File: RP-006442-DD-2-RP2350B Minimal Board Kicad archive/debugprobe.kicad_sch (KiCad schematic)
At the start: 41 parts, among them J4 Conn_01x03, J5 USB_C_Receptacle_USB2.0_16P, SW3 SW_Push, SW4 SW_Push, SW9 SW_SPDT, U5 W25Q128JVS, U6 NCP1117-3.3_SOT223, U7 RP2350_60QFN, Y2 ABM8-272-T3

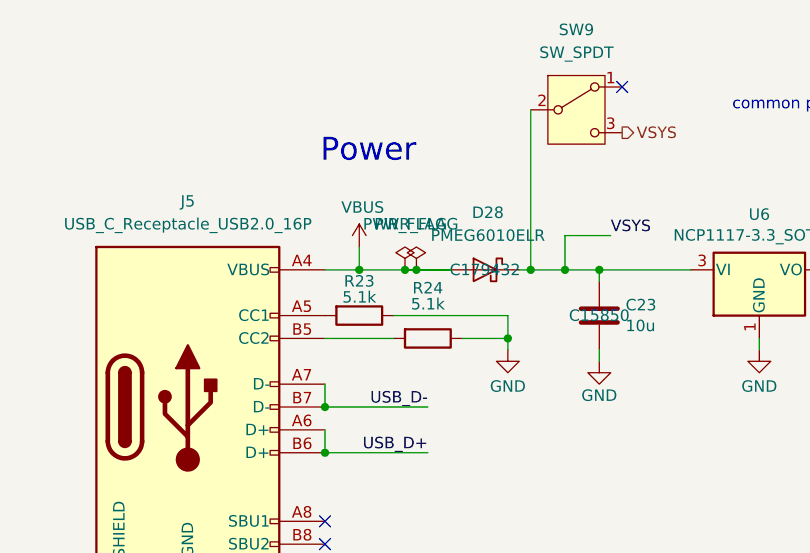
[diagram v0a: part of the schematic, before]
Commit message: Update GS3011CR-G footprint
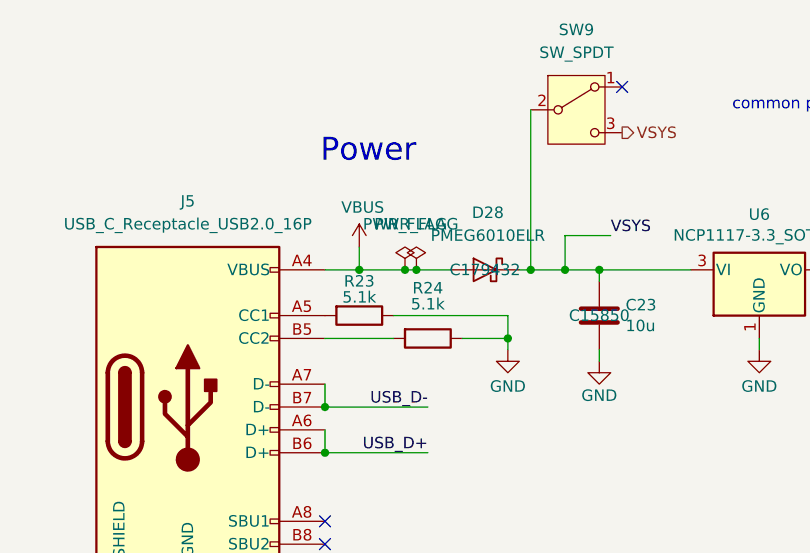
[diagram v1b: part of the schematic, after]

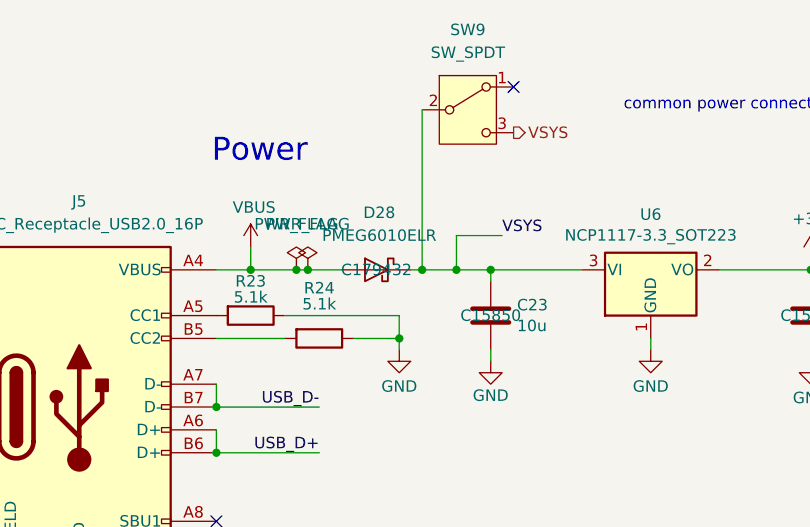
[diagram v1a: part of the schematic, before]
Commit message: Update hex display pcb traces
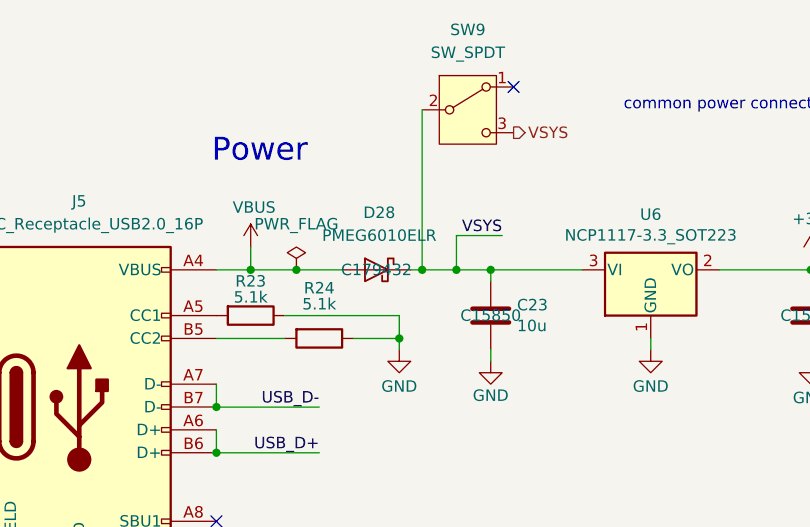
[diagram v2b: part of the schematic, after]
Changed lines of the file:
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@@
 	)
 	(junction
-		(at 76.2 58.42)
-		(diameter 0)
-		(color 0 0 0 0)
-	)
-	(junction
 		(at 209.55 100.33)
 		(diameter 0)
@@
 	)
 	(junction
-		(at 74.93 58.42)
-		(diameter 0)
-		(color 0 0 0 0)
-	)
-	(junction
 		(at 57.15 182.88)
 		(diameter 0)
@@
 	)
 	(junction
+		(at 74.93 58.42)
+		(diameter 0)
+		(color 0 0 0 0)
+	)
+	(junction
 		(at 189.23 90.17)
 		(diameter 0)
@@
 	(wire
 		(pts
-			(xy 76.2 58.42) (xy 80.01 58.42)
+			(xy 69.85 58.42) (xy 74.93 58.42)
 		)
 		(stroke
@@
 	(wire
 		(pts
+			(xy 74.93 58.42) (xy 80.01 58.42)
+		)
+		(stroke
+			(width 0)
+			(type default)
+		)
+	)
+	(wire
+		(pts
 			(xy 292.1 91.44) (xy 280.67 91.44)
 		)
@@
 	(wire
 		(pts
-			(xy 69.85 58.42) (xy 74.93 58.42)
-		)
-		(stroke
-			(width 0)
-			(type default)
-		)
-	)
-	(wire
-		(pts
 			(xy 92.71 58.42) (xy 96.52 58.42)
 		)
@@
 	(wire
 		(pts
-			(xy 74.93 58.42) (xy 76.2 58.42)
-		)
-		(stroke
-			(width 0)
-			(type default)
-		)
-	)
-	(wire
-		(pts
 			(xy 77.47 78.74) (xy 66.04 78.74)
 		)
@@
 	)
 	(label "VSYS"
-		(at 97.79 54.61 0)
+		(at 97.79 54.61 180)
 		(effects
 			(font
 				(size 1.27 1.27)
 			)
-			(justify left bottom)
+			(justify right bottom)
 		)
 	)
@@
 	(symbol
 		(lib_id "power:PWR_FLAG")
-		(at 76.2 58.42 0)
+		(at 74.93 58.42 0)
 		(unit 1)
 		(exclude_from_sim no)
@@
 		(fields_autoplaced yes)
 		(property "Reference" "#FLG02"
-			(at 76.2 56.515 0)
+			(at 74.93 56.515 0)
 			(effects
 				(font
@@
 		)
 		(property "Value" "PWR_FLAG"
-			(at 76.2 53.34 0)
+			(at 74.93 53.34 0)
 			(effects
 				(font
@@
 		)
 		(property "Footprint" ""
-			(at 76.2 58.42 0)
+			(at 74.93 58.42 0)
 			(effects
 				(font
@@
 		)
 		(property "Datasheet" "~"
-			(at 76.2 58.42 0)
+			(at 74.93 58.42 0)
 			(effects
 				(font
@@
 		)
 		(property "Description" "Special symbol for telling ERC where power comes from"
-			(at 76.2 58.42 0)
+			(at 74.93 58.42 0)
 			(effects
 				(font
@@
 		)
 		(instances
-			(project ""
+			(project "RP2350_80QFN_minimal"
 				(path "/94683f5c-9cd9-448e-be96-9792537b5cb8/500e1af8-c8c5-44c6-9fbe-f4d5e5ab4ca8"
 					(reference "#FLG02")
@@
 					(unit 1)
 				)
-			)
-		)
-	)
-	(symbol
-		(lib_id "power:PWR_FLAG")
-		(at 74.93 58.42 0)
-		(unit 1)
-		(exclude_from_sim no)
-		(in_bom yes)
-		(on_board yes)
-		(dnp no)
-		(fields_autoplaced yes)
-		(property "Reference" "#FLG02"
-			(at 74.93 56.515 0)
-			(effects
-				(font
-					(size 1.27 1.27)
-				)
-				(hide yes)
-			)
-		)
-		(property "Value" "PWR_FLAG"
-			(at 74.93 53.34 0)
-			(effects
-				(font
-					(size 1.27 1.27)
-				)
-			)
-		)
-		(property "Footprint" ""
-			(at 74.93 58.42 0)
-			(effects
-				(font
-					(size 1.27 1.27)
-				)
-				(hide yes)
-			)
-		)
-		(property "Datasheet" "~"
-			(at 74.93 58.42 0)
-			(effects
-				(font
-					(size 1.27 1.27)
-				)
-				(hide yes)
-			)
-		)
-		(property "Description" "Special symbol for telling ERC where power comes from"
-			(at 74.93 58.42 0)
-			(effects
-				(font
-					(size 1.27 1.27)
-				)
-				(hide yes)
-			)
-		)
-		(pin "1"
-		)
-		(instances
-			(project ""
-				(path "/94683f5c-9cd9-448e-be96-9792537b5cb8/500e1af8-c8c5-44c6-9fbe-f4d5e5ab4ca8"
-					(reference "#FLG02")
-					(unit 1)
-				)

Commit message: Update
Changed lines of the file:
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@@
 	(text "Power"
 		(exclude_from_sim no)
-		(at 65.532 46.736 0)
+		(at 65.024 42.926 0)
 		(effects
 			(font
@@
 	)
 	(junction
+		(at 162.56 121.92)
+		(diameter 0)
+		(color 0 0 0 0)
+	)
+	(junction
 		(at 212.09 100.33)
 		(diameter 0)
@@
 	(wire
 		(pts
+			(xy 162.56 121.92) (xy 168.91 121.92)
+		)
+		(stroke
+			(width 0)
+			(type default)
+		)
+	)
+	(wire
+		(pts
 			(xy 40.64 182.88) (xy 43.18 182.88)
 		)
@@
 	(wire
 		(pts
-			(xy 153.67 121.92) (xy 168.91 121.92)
+			(xy 153.67 121.92) (xy 162.56 121.92)
 		)
 		(stroke
@@
 					(unit 1)
 				)
+			)
+		)
+	)
+	(symbol
+		(lib_id "power:PWR_FLAG")
+		(at 162.56 121.92 0)
+		(unit 1)
+		(exclude_from_sim no)
+		(in_bom yes)
+		(on_board yes)
+		(dnp no)
+		(fields_autoplaced yes)
+		(property "Reference" "#FLG05"
+			(at 162.56 120.015 0)
+			(effects
+				(font
+					(size 1.27 1.27)
+				)
+				(hide yes)
+			)
+		)
+		(property "Value" "PWR_FLAG"
+			(at 162.56 116.84 0)
+			(effects
+				(font
+					(size 1.27 1.27)
+				)
+			)
+		)
+		(property "Footprint" ""
+			(at 162.56 121.92 0)
+			(effects
+				(font
+					(size 1.27 1.27)
+				)
+				(hide yes)
+			)
+		)
+		(property "Datasheet" "~"
+			(at 162.56 121.92 0)
+			(effects
+				(font
+					(size 1.27 1.27)
+				)
+				(hide yes)
+			)
+		)
+		(property "Description" "Special symbol for telling ERC where power comes from"
+			(at 162.56 121.92 0)
+			(effects
+				(font
+					(size 1.27 1.27)
+				)
+				(hide yes)
+			)
+		)
+		(pin "1"
+		)
+		(instances
+			(project ""
+				(path "/94683f5c-9cd9-448e-be96-9792537b5cb8/500e1af8-c8c5-44c6-9fbe-f4d5e5ab4ca8"
+					(reference "#FLG05")
+					(unit 1)
+				)

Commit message: Update usb power switch
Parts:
- SW9: footprint Button_Switch_SMD:SW_SPDT_HRO_K3-1235S-K1 -> Button_Switch_SMD:SW_SPDT_G-Switch_MK-12C03-G015; LCSC C520835 -> C2890358
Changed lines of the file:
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@@
 			)
 		)
-		(property "Footprint" "Button_Switch_SMD:SW_SPDT_HRO_K3-1235S-K1"
+		(property "Footprint" "Button_Switch_SMD:SW_SPDT_G-Switch_MK-12C03-G015"
 			(at 93.98 40.64 0)
 			(effects
@@
 			)
 		)
-		(property "LCSC" "C520835"
+		(property "LCSC" "C2890358"
 			(at 93.98 40.64 0)
 			(effects

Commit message: Production files
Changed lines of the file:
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@@
 					(size 1.27 1.27)
 				)
-				(hide yes)
 			)
 		)
@@
 			)
 		)
-		(property "LSCS" ""
-			(at 50.8 73.66 0)
-			(effects
-				(font
-					(size 1.27 1.27)
-				)
-			)
-		)
 		(pin "B5"
 		)
@@
 					(size 1.27 1.27)
 				)
-				(hide yes)
 			)
 		)
@@
 			)
 		)
-		(property "LSCS" ""
-			(at 200.66 85.09 0)
-			(effects
-				(font
-					(size 1.27 1.27)
-				)
-			)
-		)
 		(pin "1"
 		)
@@
 					(size 1.27 1.27)
 				)
-				(hide yes)
 			)
 		)
@@
 					(size 1.27 1.27)
 				)
-				(hide yes)
 			)
 		)
@@
 			)
 		)
-		(property "LSCS" ""
-			(at 177.8 85.09 0)
-			(effects
-				(font
-					(size 1.27 1.27)
-				)
-			)
-		)
 		(pin "1"
 		)
@@
 					(size 1.27 1.27)
 				)
-				(hide yes)
 			)
 		)
@@
 					(size 1.27 1.27)
 				)
-				(hide yes)
 			)
 		)
@@
 					(size 1.27 1.27)
 				)
-				(hide yes)
 			)
 		)

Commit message: Created file for switch footprint
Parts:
- SW9: footprint Button_Switch_SMD:SW_SPDT_G-Switch_MK-12C03-G015 -> MK-12C03-G015:SW_SPDT_G-Switch_MK-12C03-G015
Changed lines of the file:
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@@
 			)
 		)
-		(property "Footprint" "Button_Switch_SMD:SW_SPDT_G-Switch_MK-12C03-G015"
+		(property "Footprint" "MK-12C03-G015:SW_SPDT_G-Switch_MK-12C03-G015"
 			(at 93.98 40.64 0)
 			(effects
